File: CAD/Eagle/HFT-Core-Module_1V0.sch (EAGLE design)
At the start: 385 parts, among them Q0521 ABS07-32.768KHZ, Q0811 ABM03B-32.000MHZ, Q0911 ABM3B-16MHZ-10-R50-1-U, T1201 MMBT2222, T1202 MMBT2222, T1203 MMBT2222, U0111 STM32L4Z_144PIN_SMPS, U0431 PAM2305AAB120, U0601 LM4120IM5-3.0, U0611 MAX5217, U0631 CFPT-141-20MHZ, U0641 OPA354, U0701 Si5338, U0801 SX1276, U0901 AX5243, U0911 PE4259, U0921 PE4259, U0991 PE4259, U1011 MAX5136AGTG+, U1101 MCP3911A0-E-SS, U1121 OPA354, U1131 OPA354, U1141 OPA354, U1201 NHD-C0220BIZ_2X20CHARS, U1301 MPU-9250, U1311 MS5607-02BA03, U1321 SHT31-DIS, U1401 SOLARPANEL_3V3_5MA1_25MM_X_20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, U1402 SPV1040T, U1501 TS5A23166, U1601 PAM2305AAB330, U1701 TS5A23166, U1801 TS5A23166, U1901 TS5A23166, X1261 TTE_EN11-HSM, X2101 SMA_SMT_AMPHENOL-901-143, X2111 SMA_SMT_AMPHENOL-901-143, X2201 CUI SJ1-3535NS, X2211 CUI SJ1-3535NS, X2311 2X20/90_1MM27_HARWIN_M50-3202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, X2312 2X20/90_1MM27_HARWIN_M50-3202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, X2321 2X20/90_1MM27_HARWIN_M50-3202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, X2322 2X20/90_1MM27_HARWIN_M50-3202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, X2331 2X20/90_1MM27_HARWIN_M50-3202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, X2332 2X20/90_1MM27_HARWIN_M50-3202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

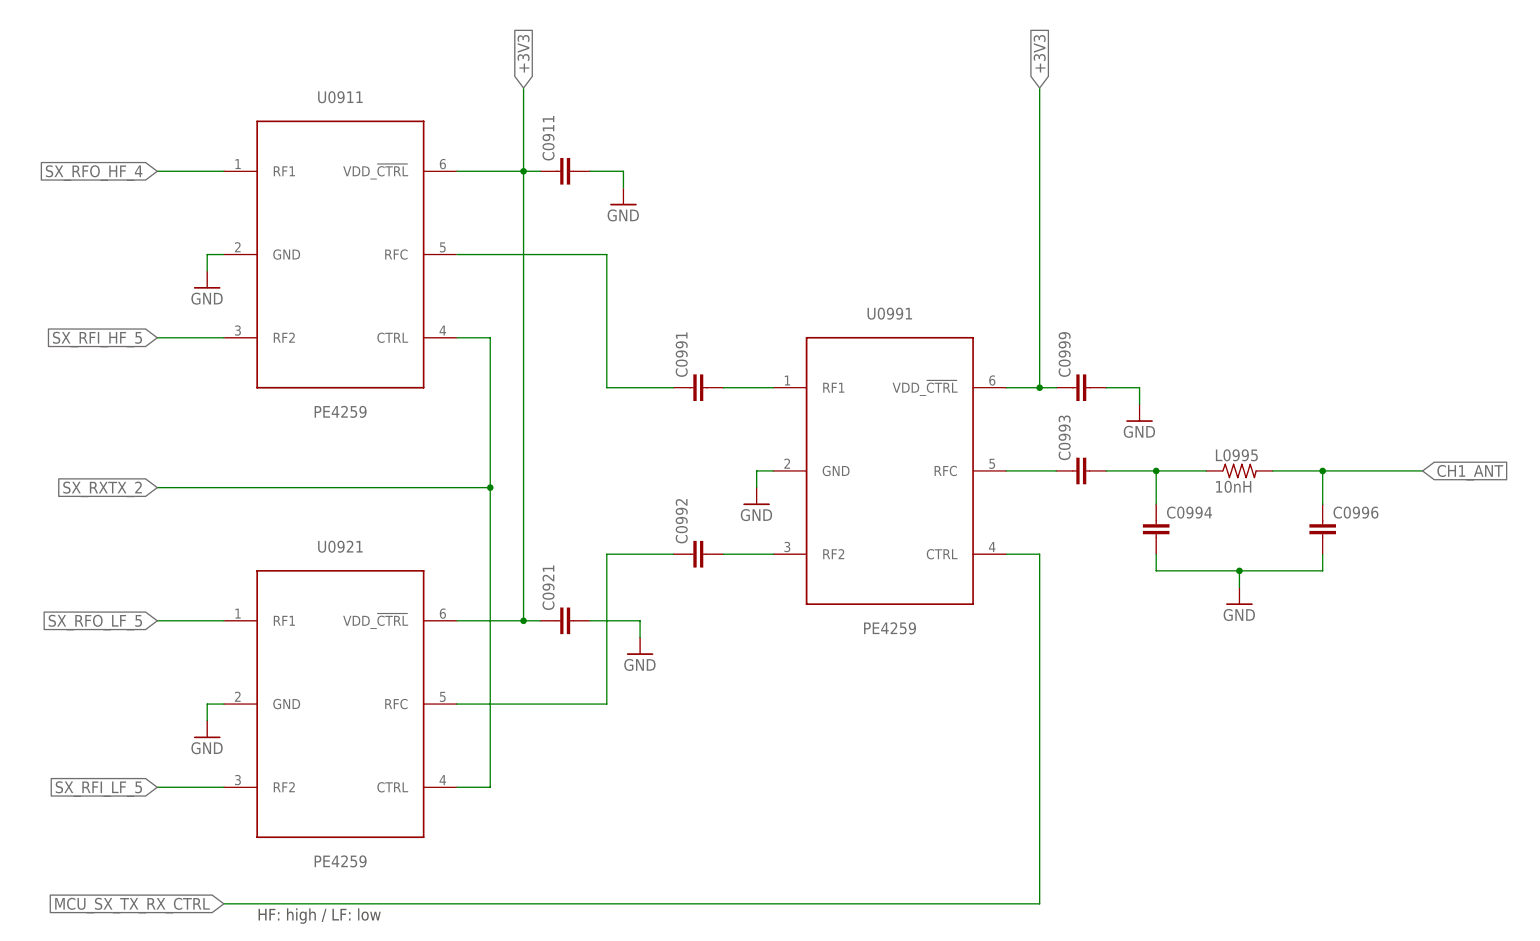
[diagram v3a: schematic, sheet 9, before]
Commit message: HW_1V0 - ERC findings fixed
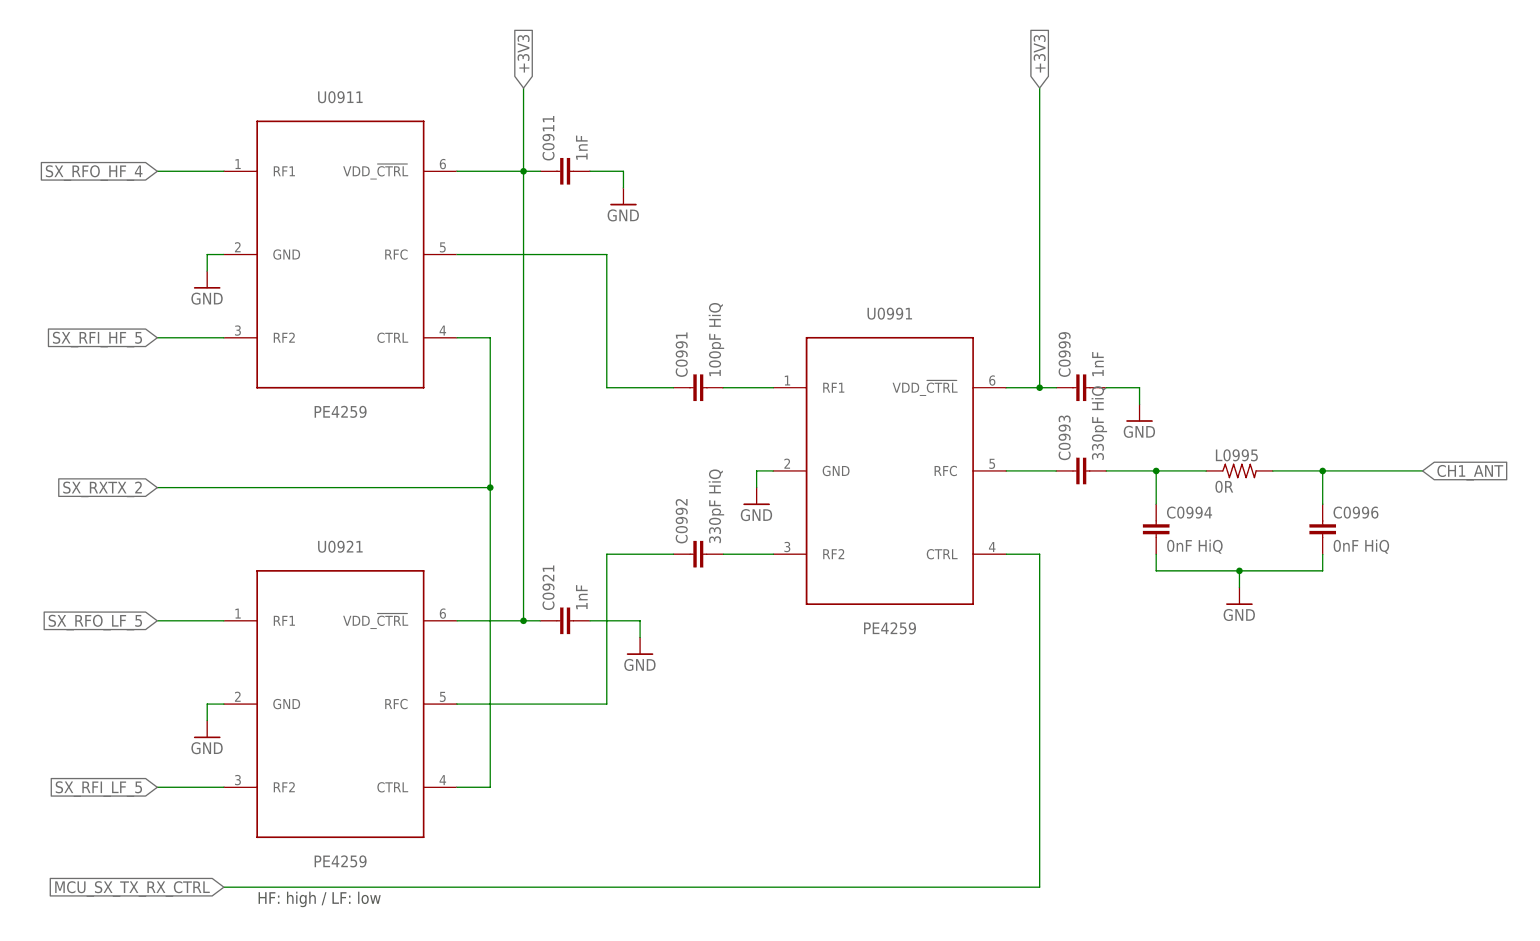
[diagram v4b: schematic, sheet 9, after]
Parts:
- C0851, C0852: value (none) -> 47pF
- C0911, C0921, C0999: value (none) -> 1nF
- C0991: value (none) -> 100pF HiQ
- C0992, C0993: value (none) -> 330pF HiQ
- C0994, C0996: value (none) -> 0nF HiQ
- L0995: value 10nH -> 0R
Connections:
- removed net I2C2_INT: R1301.2
- net PF13: now also R1301.2
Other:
- note added: "I2C2_INT"
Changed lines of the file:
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@@
 <part name="C0865" library="rcl" deviceset="C-EU" device="C0603" value="1.8pF"/>
 <part name="GND0862" library="df4iah_supply" deviceset="GND" device=""/>
-<part name="C0851" library="rcl" deviceset="C-EU" device="C0603"/>
-<part name="C0852" library="rcl" deviceset="C-EU" device="C0603"/>
+<part name="C0851" library="rcl" deviceset="C-EU" device="C0603" value="47pF"/>
+<part name="C0852" library="rcl" deviceset="C-EU" device="C0603" value="47pF"/>
 <part name="GND0851" library="df4iah_supply" deviceset="GND" device=""/>
 <part name="GND0852" library="df4iah_supply" deviceset="GND" device=""/>
@@
 <part name="U0921" library="df4iah_rf" deviceset="PE4259" device=""/>
 <part name="U0991" library="df4iah_rf" deviceset="PE4259" device=""/>
-<part name="C0991" library="rcl" deviceset="C-EU" device="C0603"/>
-<part name="C0992" library="rcl" deviceset="C-EU" device="C0603"/>
-<part name="C0993" library="rcl" deviceset="C-EU" device="C0603"/>
+<part name="C0991" library="rcl" deviceset="C-EU" device="C0603" value="100pF HiQ"/>
+<part name="C0992" library="rcl" deviceset="C-EU" device="C0603" value="330pF HiQ"/>
+<part name="C0993" library="rcl" deviceset="C-EU" device="C0603" value="330pF HiQ"/>
 <part name="GND0921" library="df4iah_supply" deviceset="GND" device=""/>
 <part name="GND0911" library="df4iah_supply" deviceset="GND" device=""/>
 <part name="GND0991" library="df4iah_supply" deviceset="GND" device=""/>
-<part name="C0994" library="rcl" deviceset="C-EU" device="C0603"/>
-<part name="C0996" library="rcl" deviceset="C-EU" device="C0603"/>
-<part name="L0995" library="rcl" deviceset="R-US_" device="R0603" value="10nH"/>
+<part name="C0994" library="rcl" deviceset="C-EU" device="C0603" value="0nF HiQ"/>
+<part name="C0996" library="rcl" deviceset="C-EU" device="C0603" value="0nF HiQ"/>
+<part name="L0995" library="rcl" deviceset="R-US_" device="R0603" value="0R"/>
 <part name="GND0992" library="df4iah_supply" deviceset="GND" device=""/>
-<part name="C0911" library="rcl" deviceset="C-EU" device="C0603"/>
-<part name="C0921" library="rcl" deviceset="C-EU" device="C0603"/>
+<part name="C0911" library="rcl" deviceset="C-EU" device="C0603" value="1nF"/>
+<part name="C0921" library="rcl" deviceset="C-EU" device="C0603" value="1nF"/>
 <part name="GND0912" library="df4iah_supply" deviceset="GND" device=""/>
 <part name="GND0922" library="df4iah_supply" deviceset="GND" device=""/>
-<part name="C0999" library="rcl" deviceset="C-EU" device="C0603"/>
+<part name="C0999" library="rcl" deviceset="C-EU" device="C0603" value="1nF"/>
 <part name="GND0999" library="df4iah_supply" deviceset="GND" device=""/>
 <part name="R0277" library="rcl" deviceset="R-EU_" device="R0603" value="47R"/>
@@
 <description>VHF/UHF SX1276 - ch 1 - HF sw</description>
 <plain>
-<text x="50.8" y="22.86" size="1.778" layer="97">HF: high / LF: low</text>
+<text x="50.8" y="25.4" size="1.778" layer="97">HF: high / LF: low</text>
 </plain>
 <instances>
@@
 <pinref part="U0991" gate="G$1" pin="CTRL"/>
 <wire x1="165.1" y1="78.74" x2="170.18" y2="78.74" width="0.1524" layer="91"/>
-<wire x1="170.18" y1="78.74" x2="170.18" y2="25.4" width="0.1524" layer="91"/>
-<wire x1="170.18" y1="25.4" x2="45.72" y2="25.4" width="0.1524" layer="91"/>
-<label x="45.72" y="25.4" size="1.778" layer="95" rot="R180" xref="yes"/>
+<wire x1="170.18" y1="78.74" x2="170.18" y2="27.94" width="0.1524" layer="91"/>
+<wire x1="170.18" y1="27.94" x2="45.72" y2="27.94" width="0.1524" layer="91"/>
+<label x="45.72" y="27.94" size="1.778" layer="95" rot="R180" xref="yes"/>
 </segment>
 </net>
@@
 <text x="160.02" y="93.98" size="1.778" layer="97">I2C address = 1000100</text>
 <text x="195.58" y="81.28" size="2.54" layer="97" ratio="15">I2C4 Termination</text>
+<text x="127" y="25.4" size="1.778" layer="97">I2C2_INT</text>
 </plain>
 <instances>
@@
 </segment>
 </net>
-<net name="I2C2_INT" class="0">
-<segment>
-<label x="142.24" y="25.4" size="1.778" layer="95" xref="yes"/>
-<pinref part="R1301" gate="G$1" pin="2"/>
-<wire x1="101.6" y1="25.4" x2="142.24" y2="25.4" width="0.1524" layer="91"/>
-</segment>
-</net>
 <net name="MPU_INT" class="0">
 <segment>
@@
 </segment>
 </net>
+<net name="PF13" class="0">
+<segment>
+<label x="142.24" y="25.4" size="1.778" layer="95" xref="yes"/>
+<pinref part="R1301" gate="G$1" pin="2"/>
+<wire x1="101.6" y1="25.4" x2="142.24" y2="25.4" width="0.1524" layer="91"/>
+</segment>
+</net>

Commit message: HW_1V0 - component labels placed
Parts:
- added TP_SX_DIO0, TP_SX_DIO1, TP_SX_DIO2, TP_SX_DIO3, TP_SX_DIO4, TP_SX_DIO5, TP_SX_RXTX: PTR1TP06R, testpad:PTR1TP06R
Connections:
- net SX_DIO0: now also TP_SX_DIO0.TP
- net SX_DIO1: now also TP_SX_DIO1.TP
- net SX_DIO2: now also TP_SX_DIO2.TP
- net SX_DIO3: now also TP_SX_DIO3.TP
- net SX_DIO4: now also TP_SX_DIO4.TP
- net SX_DIO5: now also TP_SX_DIO5.TP
- net SX_RXTX: now also TP_SX_RXTX.TP
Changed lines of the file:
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@@
 <part name="GND0999" library="df4iah_supply" deviceset="GND" device=""/>
 <part name="R0277" library="rcl" deviceset="R-EU_" device="R0603" value="47R"/>
+<part name="TP_SX_DIO5" library="testpad" deviceset="PTR1" device="TP06R"/>
+<part name="TP_SX_DIO4" library="testpad" deviceset="PTR1" device="TP06R"/>
+<part name="TP_SX_DIO3" library="testpad" deviceset="PTR1" device="TP06R"/>
+<part name="TP_SX_DIO2" library="testpad" deviceset="PTR1" device="TP06R"/>
+<part name="TP_SX_DIO1" library="testpad" deviceset="PTR1" device="TP06R"/>
+<part name="TP_SX_DIO0" library="testpad" deviceset="PTR1" device="TP06R"/>
+<part name="TP_SX_RXTX" library="testpad" deviceset="PTR1" device="TP06R"/>
 </parts>
 <sheets>
@@
 <instance part="R0804" gate="G$1" x="170.18" y="48.26"/>
 <instance part="R0806" gate="G$1" x="170.18" y="38.1"/>
+<instance part="TP_SX_DIO5" gate="G$1" x="129.54" y="12.7"/>
+<instance part="TP_SX_DIO4" gate="G$1" x="132.08" y="20.32"/>
+<instance part="TP_SX_DIO3" gate="G$1" x="134.62" y="12.7"/>
+<instance part="TP_SX_DIO2" gate="G$1" x="137.16" y="20.32"/>
+<instance part="TP_SX_DIO1" gate="G$1" x="139.7" y="12.7"/>
+<instance part="TP_SX_DIO0" gate="G$1" x="142.24" y="20.32"/>
+<instance part="TP_SX_RXTX" gate="G$1" x="144.78" y="12.7"/>
 </instances>
 <busses>
@@
 <pinref part="R0801" gate="G$1" pin="1"/>
 <wire x1="144.78" y1="63.5" x2="149.86" y2="63.5" width="0.1524" layer="91"/>
+<pinref part="TP_SX_RXTX" gate="G$1" pin="TP"/>
+<wire x1="144.78" y1="63.5" x2="144.78" y2="15.24" width="0.1524" layer="91"/>
+<junction x="144.78" y="63.5"/>
 </segment>
 </net>
@@
 <wire x1="142.24" y1="58.42" x2="165.1" y2="58.42" width="0.1524" layer="91"/>
 <pinref part="R0802" gate="G$1" pin="1"/>
+<pinref part="TP_SX_DIO0" gate="G$1" pin="TP"/>
+<wire x1="142.24" y1="58.42" x2="142.24" y2="22.86" width="0.1524" layer="91"/>
+<junction x="142.24" y="58.42"/>
 </segment>
 </net>
@@
 <wire x1="139.7" y1="53.34" x2="149.86" y2="53.34" width="0.1524" layer="91"/>
 <pinref part="R0803" gate="G$1" pin="1"/>
+<pinref part="TP_SX_DIO1" gate="G$1" pin="TP"/>
+<wire x1="139.7" y1="53.34" x2="139.7" y2="15.24" width="0.1524" layer="91"/>
+<junction x="139.7" y="53.34"/>
 </segment>
 </net>
@@
 <wire x1="137.16" y1="48.26" x2="165.1" y2="48.26" width="0.1524" layer="91"/>
 <pinref part="R0804" gate="G$1" pin="1"/>
+<pinref part="TP_SX_DIO2" gate="G$1" pin="TP"/>
+<wire x1="137.16" y1="48.26" x2="137.16" y2="22.86" width="0.1524" layer="91"/>
+<junction x="137.16" y="48.26"/>
 </segment>
 </net>
@@
 <wire x1="134.62" y1="43.18" x2="149.86" y2="43.18" width="0.1524" layer="91"/>
 <pinref part="R0805" gate="G$1" pin="1"/>
+<pinref part="TP_SX_DIO3" gate="G$1" pin="TP"/>
+<wire x1="134.62" y1="43.18" x2="134.62" y2="15.24" width="0.1524" layer="91"/>
+<junction x="134.62" y="43.18"/>
 </segment>
 </net>
@@
 <wire x1="132.08" y1="38.1" x2="165.1" y2="38.1" width="0.1524" layer="91"/>
 <pinref part="R0806" gate="G$1" pin="1"/>
+<pinref part="TP_SX_DIO4" gate="G$1" pin="TP"/>
+<wire x1="132.08" y1="38.1" x2="132.08" y2="22.86" width="0.1524" layer="91"/>
+<junction x="132.08" y="38.1"/>
 </segment>
 </net>
@@
 <wire x1="129.54" y1="33.02" x2="149.86" y2="33.02" width="0.1524" layer="91"/>
 <pinref part="R0807" gate="G$1" pin="1"/>
+<pinref part="TP_SX_DIO5" gate="G$1" pin="TP"/>
+<wire x1="129.54" y1="33.02" x2="129.54" y2="15.24" width="0.1524" layer="91"/>
+<junction x="129.54" y="33.02"/>
 </segment>
 </net>

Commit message: HW_1V0 - routing of RF and some of power management done
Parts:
- renumbered C_AX1_A2 to C_AX_A2, C_AX1_A3 to C_AX_A3, C_AX1_B2 to C_AX_B2, C_AX1_C1 to C_AX_C1, C_AX1_C2 to C_AX_C2, C_AX1_F2 to C_AX_F2, C_AX1_M1 to C_AX_M1, C_AX1_M2 to C_AX_M2, C_AX1_T1 to C_AX_T1, C_AX1_T2 to C_AX_T2, L_AX1_1 to L_AX_1, L_AX1_B1 to L_AX_B1, L_AX1_B2 to L_AX_B2, L_AX1_C1 to L_AX_C1, L_AX1_C2 to L_AX_C2, L_AX1_F1 to L_AX_F1, L_AX1_T1 to L_AX_T1, L_AX1_T2 to L_AX_T2, TP_AX1_ADC1 to TP_AX_ADC1, TP_AX1_ADC2 to TP_AX_ADC2, TP_AX1_IRQ to TP_AX_IRQ, TP_AX1_TCXO_EN to TP_AX_TCXO_EN
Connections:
- net AX1_ADC1 renamed AX_ADC1
- net AX1_ADC2 renamed AX_ADC2
- net AX1_ANTN renamed AX_ANTN
- net AX1_ANTP renamed AX_ANTP
- net AX1_B1 renamed AX_B1
- net AX1_B2 renamed AX_B2
- net AX1_CLK16N renamed AX_CLK16N
- net AX1_CLK16P renamed AX_CLK16P
- net AX1_COMB renamed AX_COMB
- net AX1_L1 renamed AX_L1
- net AX1_L2 renamed AX_L2
- net AX1_T1 renamed AX_T1
- net AX1_T2 renamed AX_T2
- net AX1_VDD1 renamed AX_VDD1
- net AX1_VDD5 renamed AX_VDD5
- net MCU_AX1_MISO renamed MCU_AX_MISO

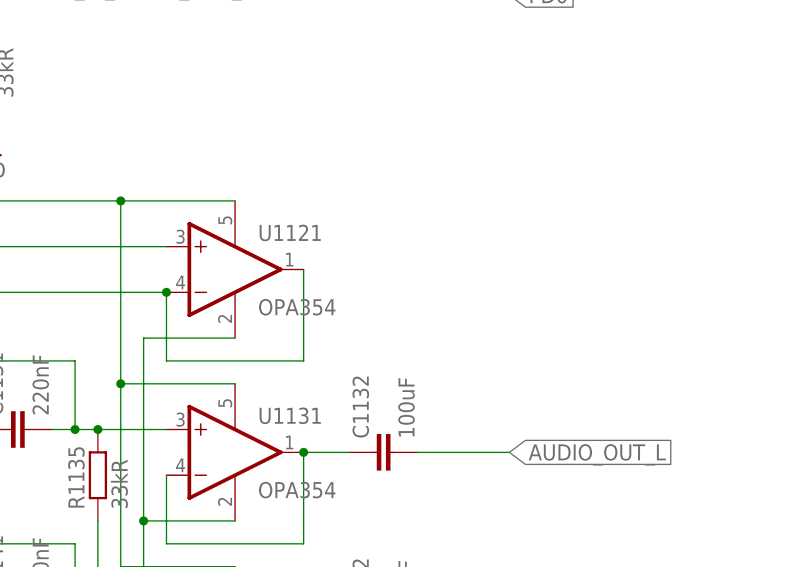
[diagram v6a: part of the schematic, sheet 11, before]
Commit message: HW_1V0 - many more lines added
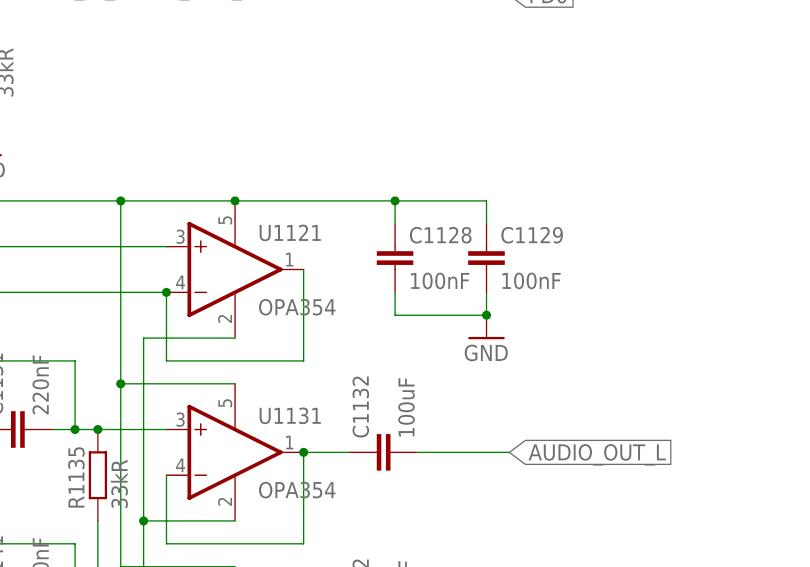
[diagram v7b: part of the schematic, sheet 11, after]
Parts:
- added C1128, C1129: 100nF, df4iah_rcl:C-EUC0603
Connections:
- net CLK0N renamed CLK0_N
- net CLK0P renamed CLK0_P
- net CLK1N renamed CLK1_N
- net CLK1P renamed CLK1_P
- net CLK2N renamed CLK2_N
- net CLK2P renamed CLK2_P
- net PA11 renamed PA_USB_N
- net PA12 renamed PA_USB_P
- net +3V3_HICUR: now also C1128.1, C1129.1
- net GND: now also C1128.2, C1129.2
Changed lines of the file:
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@@
 <part name="TP_SX_DIO0" library="testpad" deviceset="PTR1" device="TP06R"/>
 <part name="TP_SX_RXTX" library="testpad" deviceset="PTR1" device="TP06R"/>
+<part name="C1129" library="df4iah_rcl" deviceset="C-EU" device="C0603" value="100nF"/>
+<part name="GND1122" library="df4iah_supply" deviceset="GND" device=""/>
+<part name="C1128" library="df4iah_rcl" deviceset="C-EU" device="C0603" value="100nF"/>
 </parts>
 <sheets>
@@
 </segment>
 </net>
-<net name="PA12" class="0">
+<net name="PA_USB_P" class="0">
 <segment>
 <pinref part="U0111" gate="G$1" pin="PA12"/>
@@
 </segment>
 </net>
-<net name="PA11" class="0">
+<net name="PA_USB_N" class="0">
 <segment>
 <pinref part="U0111" gate="G$1" pin="PA11"/>
@@
 </segment>
 </net>
-<net name="CLK1N" class="0">
+<net name="CLK1_N" class="0">
 <segment>
 <pinref part="R0735" gate="G$1" pin="2"/>
@@
 </segment>
 </net>
-<net name="CLK1P" class="0">
+<net name="CLK1_P" class="0">
 <segment>
 <pinref part="R0736" gate="G$1" pin="2"/>
@@
 </segment>
 </net>
-<net name="CLK2P" class="0">
+<net name="CLK2_P" class="0">
 <segment>
 <pinref part="R0732" gate="G$1" pin="2"/>
@@
 </segment>
 </net>
-<net name="CLK2N" class="0">
+<net name="CLK2_N" class="0">
 <segment>
 <pinref part="R0731" gate="G$1" pin="2"/>
@@
 </segment>
 </net>
-<net name="CLK0P" class="0">
+<net name="CLK0_P" class="0">
 <segment>
 <pinref part="R0744" gate="G$1" pin="2"/>
@@
 </segment>
 </net>
-<net name="CLK0N" class="0">
+<net name="CLK0_N" class="0">
 <segment>
 <pinref part="R0743" gate="G$1" pin="2"/>
@@
 <instance part="R1110" gate="G$1" x="152.4" y="99.06" rot="R90"/>
 <instance part="GND1103" gate="1" x="152.4" y="88.9"/>
+<instance part="C1129" gate="G$1" x="208.28" y="78.74"/>
+<instance part="GND1122" gate="1" x="208.28" y="68.58"/>
+<instance part="C1128" gate="G$1" x="198.12" y="78.74"/>
 </instances>
 <busses>
@@
 <wire x1="152.4" y1="91.44" x2="152.4" y2="93.98" width="0.1524" layer="91"/>
 </segment>
+<segment>
+<pinref part="C1129" gate="G$1" pin="2"/>
+<wire x1="208.28" y1="73.66" x2="208.28" y2="71.12" width="0.1524" layer="91"/>
+<pinref part="GND1122" gate="1" pin="GND"/>
+<wire x1="208.28" y1="71.12" x2="198.12" y2="71.12" width="0.1524" layer="91"/>
+<pinref part="C1128" gate="G$1" pin="2"/>
+<wire x1="198.12" y1="71.12" x2="198.12" y2="73.66" width="0.1524" layer="91"/>
+<junction x="208.28" y="71.12"/>
+</segment>
 </net>
 <net name="MAX5136_REF" class="0">
@@
 <wire x1="167.64" y1="83.82" x2="180.34" y2="83.82" width="0.1524" layer="91"/>
 <junction x="167.64" y="83.82"/>
+<pinref part="C1129" gate="G$1" pin="1"/>
+<wire x1="180.34" y1="83.82" x2="198.12" y2="83.82" width="0.1524" layer="91"/>
+<wire x1="198.12" y1="83.82" x2="208.28" y2="83.82" width="0.1524" layer="91"/>
+<wire x1="208.28" y1="83.82" x2="208.28" y2="81.28" width="0.1524" layer="91"/>
+<pinref part="C1128" gate="G$1" pin="1"/>
+<wire x1="198.12" y1="83.82" x2="198.12" y2="81.28" width="0.1524" layer="91"/>
+<junction x="198.12" y="83.82"/>
+<junction x="180.34" y="83.82"/>
 </segment>
 <segment>
@@
 </segment>
 </net>
-<net name="PA11" class="0">
+<net name="PA_USB_N" class="0">
 <segment>
 <pinref part="X2001" gate="G$1" pin="J_D-"/>
@@
 </segment>
 </net>
-<net name="PA12" class="0">
+<net name="PA_USB_P" class="0">
 <segment>
 <pinref part="X2001" gate="G$1" pin="J_D+"/>
@@
 </segment>
 </net>
-<net name="CLK0P" class="0">
+<net name="CLK0_P" class="0">
 <segment>
 <wire x1="139.7" y1="35.56" x2="137.16" y2="38.1" width="0.1524" layer="91"/>
@@
 </segment>
 </net>
-<net name="CLK0N" class="0">
+<net name="CLK0_N" class="0">
 <segment>
 <wire x1="142.24" y1="35.56" x2="139.7" y2="38.1" width="0.1524" layer="91"/>
@@
 </segment>
 </net>
-<net name="CLK1P" class="0">
+<net name="CLK1_P" class="0">
 <segment>
 <wire x1="139.7" y1="83.82" x2="137.16" y2="86.36" width="0.1524" layer="91"/>
@@
 </segment>
 </net>
-<net name="CLK1N" class="0">
+<net name="CLK1_N" class="0">
 <segment>
 <wire x1="142.24" y1="83.82" x2="139.7" y2="86.36" width="0.1524" layer="91"/>
@@
 </segment>
 </net>
-<net name="CLK2P" class="0">
+<net name="CLK2_P" class="0">
 <segment>
 <wire x1="139.7" y1="132.08" x2="137.16" y2="134.62" width="0.1524" layer="91"/>
@@
 </segment>
 </net>
-<net name="CLK2N" class="0">
+<net name="CLK2_N" class="0">
 <segment>
 <wire x1="142.24" y1="132.08" x2="139.7" y2="134.62" width="0.1524" layer="91"/>
